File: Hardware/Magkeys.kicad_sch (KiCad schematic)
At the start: 169 parts, among them SW1 SW_Push, SW10 SW_Push, SW11 SW_Push, SW12 SW_Push, SW13 SW_Push, SW14 SW_Push, SW15 SW_Push, SW16 SW_Push, SW17 SW_Push, SW18 SW_Push, SW19 SW_Push, SW2 SW_Push, SW20 SW_Push, SW21 SW_Push, SW22 SW_Push, SW23 SW_Push, SW24 SW_Push, SW25 SW_Push, SW26 SW_Push, SW27 SW_Push, SW28 SW_Push, SW29 SW_Push, SW3 SW_Push, SW30 SW_Push, SW31 SW_Push, SW32 SW_Push, SW33 SW_Push, SW34 SW_Push, SW35 SW_Push, SW36 SW_Push, SW37 SW_Push, SW38 SW_Push, SW39 SW_Push, SW4 SW_Push, SW40 SW_Push, SW41 SW_Push, SW42 SW_Push, SW43 SW_Push, SW44 SW_Push, SW45 SW_Push, SW46 SW_Push, SW47 SW_Push, SW48 SW_Push, SW49 SW_Push, SW5 SW_Push, SW50 SW_Push, SW51 SW_Push, SW52 SW_Push, SW53 SW_Push, SW54 SW_Push, SW55 SW_Push, SW56 SW_Push, SW57 SW_Push, SW58 SW_Push, SW59 SW_Push, SW6 SW_Push, SW60 SW_Push, SW61 SW_Push, SW62 SW_Push, SW63 SW_Push, SW64 SW_Push, SW65 SW_Push, SW66 SW_Push, SW67 SW_Push, SW68 SW_Push, SW69 SW_Push, SW7 SW_Push, SW70 SW_Push, SW71 SW_Push, SW72 SW_Push, SW73 SW_Push, SW74 SW_Push, SW75 SW_Push, SW76 SW_Push, SW77 SW_Push, SW78 SW_Push, SW79 SW_Push, SW8 SW_Push, SW80 SW_Push, SW81 SW_Push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

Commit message: did layout
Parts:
- A1: footprint Module:RaspberryPi_Pico_W_SMD_HandSolder -> Module:RaspberryPi_Pico_W_SMD
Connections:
- net at D22.2 (A): now also SW22.1
- net at D6.2 (A): now also SW6.1
- net at D83.2 (A): now also SW83.1
- net at D51.2 (A): now also SW51.1
- net at D40.2 (A): now also SW40.1
- net at SW37.1: now also D37.2 (A)
- net at SW66.1: now also D66.2 (A)
- net at D36.2 (A): now also SW36.1
- net at SW55.1: now also D55.2 (A)
- net at D80.2 (A): now also SW80.1
- net at SW69.1: now also D69.2 (A)
- net at D52.2 (A): now also SW52.1
- net at SW21.1: now also D21.2 (A)
- net at SW25.1: now also D25.2 (A)
- net at SW79.1: now also D79.2 (A)
- net at SW65.1: now also D65.2 (A)
- net at SW9.1: now also D9.2 (A)
- net +3V3: now reaches A1.36 (3V3)
- net at D5.2 (A): now also SW5.1
- no-connect marks 2 -> 5
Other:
- moved on the sheet: D21, D22, D25, D36, D37, D40, D5, D51, D52, D55, D6, D65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

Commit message: idk
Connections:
- net COL1: now also A1.27 (GPIO21); no longer A1.21 (GPIO16)
- net COL2: now also A1.26 (GPIO20); no longer A1.22 (GPIO17)
- net COL3: now also A1.25 (GPIO19); no longer A1.24 (GPIO18)
- net COL4: now also A1.24 (GPIO18); no longer A1.25 (GPIO19)
- net COL5: now also A1.22 (GPIO17); no longer A1.26 (GPIO20)
- net COL6: now also A1.21 (GPIO16); no longer A1.27 (GPIO21)
- net ROW1: now also A1.20 (GPIO15); no longer A1.1 (GPIO0)
- net ROW10: now also A1.9 (GPIO6); no longer A1.12 (GPIO9)
- net ROW11: now also A1.7 (GPIO5); no longer A1.14 (GPIO10)
- net ROW12: now also A1.6 (GPIO4); no longer A1.15 (GPIO11)
- net ROW13: now also A1.5 (GPIO3); no longer A1.16 (GPIO12)
- net ROW14: now also A1.4 (GPIO2); no longer A1.17 (GPIO13)
- net ROW15: now also A1.2 (GPIO1); no longer A1.19 (GPIO14)
- net ROW16: now also A1.1 (GPIO0); no longer A1.20 (GPIO15)
- net ROW2: now also A1.19 (GPIO14); no longer A1.2 (GPIO1)
- net ROW3: now also A1.17 (GPIO13); no longer A1.4 (GPIO2)
- net ROW4: now also A1.16 (GPIO12); no longer A1.5 (GPIO3)
- net ROW5: now also A1.15 (GPIO11); no longer A1.6 (GPIO4)
- net ROW6: now also A1.14 (GPIO10); no longer A1.7 (GPIO5)
- net ROW7: now also A1.12 (GPIO9); no longer A1.9 (GPIO6)
- net ROW8: now also A1.11 (GPIO8); no longer A1.10 (GPIO7)
- net ROW9: now also A1.10 (GPIO7); no longer A1.11 (GPIO8)
- no-connect marks 5 -> 4
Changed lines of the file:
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@@
-	)
-	(no_connect
-		(at 487.68 91.44)
 	)
 	(no_connect
@@
 	)
 	(label "COL6"
-		(at 533.4 111.76 0)
+		(at 533.4 99.06 0)
 		(effects
 			(font
@@
 	)
 	(label "COL1"
-		(at 533.4 99.06 0)
+		(at 533.4 111.76 0)
 		(effects
 			(font
@@
 	)
 	(label "ROW16"
-		(at 487.68 134.62 180)
+		(at 487.68 96.52 180)
 		(effects
 			(font
@@
 	)
 	(label "ROW8"
-		(at 487.68 114.3 180)
+		(at 487.68 116.84 180)
 		(effects
 			(font
@@
 	)
 	(label "ROW14"
-		(at 487.68 129.54 180)
+		(at 487.68 101.6 180)
 		(effects
 			(font
@@
 	)
 	(label "ROW13"
-		(at 487.68 127 180)
+		(at 487.68 104.14 180)
 		(effects
 			(font
@@
 	)
 	(label "ROW6"
-		(at 487.68 109.22 180)
+		(at 487.68 121.92 180)
 		(effects
 			(font
@@
 	)
 	(label "COL2"
-		(at 533.4 101.6 0)
+		(at 533.4 109.22 0)
 		(effects
 			(font
@@
 	)
 	(label "ROW11"
-		(at 487.68 121.92 180)
+		(at 487.68 109.22 180)
 		(effects
 			(font
@@
 	)
 	(label "COL5"
-		(at 533.4 109.22 0)
+		(at 533.4 101.6 0)
 		(effects
 			(font
@@
 	)
 	(label "COL3"
-		(at 533.4 104.14 0)
+		(at 533.4 106.68 0)
 		(effects
 			(font
@@
 	)
 	(label "ROW10"
-		(at 487.68 119.38 180)
+		(at 487.68 111.76 180)
 		(effects
 			(font
@@
 	)
 	(label "ROW4"
-		(at 487.68 104.14 180)
+		(at 487.68 127 180)
 		(effects
 			(font
@@
 	)
 	(label "ROW12"
-		(at 487.68 124.46 180)
+		(at 487.68 106.68 180)
 		(effects
 			(font
@@
 	)
 	(label "ROW15"
-		(at 487.68 132.08 180)
+		(at 487.68 99.06 180)
 		(effects
 			(font
@@
 	)
 	(label "ROW9"
-		(at 487.68 116.84 180)
+		(at 487.68 114.3 180)
 		(effects
 			(font
@@
 	)
 	(label "ROW7"
-		(at 487.68 111.76 180)
+		(at 487.68 119.38 180)
 		(effects
 			(font
@@
 	)
 	(label "ROW3"
-		(at 487.68 101.6 180)
+		(at 487.68 129.54 180)
 		(effects
 			(font
@@
 	)
 	(label "ROW1"
-		(at 487.68 96.52 180)
+		(at 487.68 134.62 180)
 		(effects
 			(font
@@
 	)
 	(label "COL4"
-		(at 533.4 106.68 0)
+		(at 533.4 104.14 0)
 		(effects
 			(font
@@
 	)
 	(label "ROW2"
-		(at 487.68 99.06 180)
+		(at 487.68 132.08 180)
 		(effects
 			(font
@@
 	)
 	(label "ROW5"
-		(at 487.68 106.68 180)
-		(effects
-			(font
+		(at 487.68 124.46 180)
+		(effects
+			(font

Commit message: Added numpad
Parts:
- added D100, D101, D85, D86, D87, D88, D89, D90, D91, D92, D93, D94, D95, D96, D97, D98, D99: 1N4148W, Diode_SMD:D_SOD-123, symbol Diode:1N4148W
- added SW100: SW_Push, Button_Switch_Keyboard:SW_Cherry_MX_2.00u_Plate, symbol Switch:SW_Push
- added SW101, SW85, SW86, SW87, SW88, SW89, SW90, SW91, SW93, SW94, SW95, SW96, SW97, SW98: SW_Push, Button_Switch_Keyboard:SW_Cherry_MX_1.00u_Plate, symbol Switch:SW_Push
- added SW92, SW99: SW_Push, Button_Switch_Keyboard:SW_Cherry_MX_2.00u_Vertical_Plate, symbol Switch:SW_Push
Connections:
- new net: D89.2 (A), SW89.1
- new net: D100.2 (A), SW100.1
- new net: D97.2 (A), SW97.1
- new net: D85.2 (A), SW85.1
- new net: D101.2 (A), SW101.1
- new net: D94.2 (A), SW94.1
- new net: D93.2 (A), SW93.1
- new net: D96.2 (A), SW96.1
- new net: D91.2 (A), SW91.1
- new net: D90.2 (A), SW90.1
- new net: D87.2 (A), SW87.1
- new net: D95.2 (A), SW95.1
- new net: D88.2 (A), SW88.1
- new net: D99.2 (A), SW99.1
- new net: D86.2 (A), SW86.1
- new net: D92.2 (A), SW92.1
- new net: D98.2 (A), SW98.1
- new net NUM_COL1: SW100.2, SW85.2, SW89.2, SW93.2, SW96.2
- new net NUM_COL2: SW101.2, SW86.2, SW90.2, SW94.2, SW97.2
- new net NUM_COL3: SW87.2, SW91.2, SW95.2, SW98.2
- new net NUM_COL4: SW88.2, SW92.2, SW99.2
- new net NUM_ROW1: D85.1 (K), D86.1 (K), D87.1 (K), D88.1 (K)
- new net NUM_ROW2: D89.1 (K), D90.1 (K), D91.1 (K), D92.1 (K)
- new net NUM_ROW3: D93.1 (K), D94.1 (K), D95.1 (K)
- new net NUM_ROW4: D96.1 (K), D97.1 (K), D98.1 (K), D99.1 (K)
- new net NUM_ROW5: D100.1 (K), D101.1 (K)
- no-connect marks 4 -> 5
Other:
- moved on the sheet: A1

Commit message: Completed PCB
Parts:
- added U1: Seeeduino Xiao rp2040, PCM_marbastlib-xp-promicroish:Xiao_rp2040_AC_Reflow, symbol PCM_marbastlib-promicroish:Seeeduino_Xiao_rp2040
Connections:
- net +3V3: now also U1.10 (3V3)
- net GND: now also U1.18 (GND), U1.22 (GND), U1.9 (GND)
- net NUM_COL1: now also U1.11 (P3)
- net NUM_COL2: now also U1.12 (P4)
- net NUM_COL3: now also U1.13 (P2)
- net NUM_COL4: now also U1.14 (P1)
- net NUM_ROW1: now also U1.3 (P28)
- net NUM_ROW2: now also U1.4 (P29)
- net NUM_ROW3: now also U1.5 (P6)
- net NUM_ROW4: now also U1.6 (P7)
- net NUM_ROW5: now also U1.7 (P0)
- net VBUS: now also U1.17 (VIN)
- new net +5V: U1.8 (5V)
- no-connect marks 5 -> 8

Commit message: changes in the PCB
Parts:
- removed U1: Seeeduino Xiao rp2040, PCM_marbastlib-xp-promicroish:Xiao_rp2040_AC_Reflow, symbol PCM_marbastlib-promicroish:Seeeduino_Xiao_rp2040
- added J1: Conn_01x04_Pin, Connector_PinHeader_2.54mm:PinHeader_1x04_P2.54mm_Vertical, symbol Connector:Conn_01x04_Pin
- added SW102: RotaryEncoder, Rotary_Encoder:RotaryEncoder_Alps_EC11E_Vertical_H20mm, symbol Device:RotaryEncoder
- SW1, SW10, SW101, SW11, SW12, SW13, SW14, SW15, SW16, SW17, SW18, SW19, SW2, SW20, SW21, SW22, SW23, SW24, SW25, SW26, SW27, SW28, SW29, SW3, SW31, SW33, SW34, SW35, SW36, SW37, SW38, SW39, SW4, SW40, SW41, SW42, SW43, SW44, SW46, SW48, SW49, SW5, SW50, SW51, SW52, SW53, SW54, SW55, SW56, SW57, SW58, SW6, SW60, SW62, SW63, SW64, SW65, SW66, SW67, SW68, SW69, SW7, SW70, SW71, SW73, SW74, SW79, SW8, SW80, SW81, SW82, SW83, SW84, SW85, SW86, SW87, SW88, SW89, SW9, SW90, SW91, SW93, SW94, SW95, SW96, SW97, SW98: footprint Button_Switch_Keyboard:SW_Cherry_MX_1.00u_Plate -> easyeda2kicad:SW_Cherry_MX_1.00u_Plate
- SW100, SW30: footprint Button_Switch_Keyboard:SW_Cherry_MX_2.00u_Plate -> easyeda2kicad:SW_Cherry_MX_2.00u_Plate
- SW32, SW45: footprint Button_Switch_Keyboard:SW_Cherry_MX_1.50u_Plate -> easyeda2kicad:SW_Cherry_MX_1.50u_Plate
- SW47, SW72: footprint Button_Switch_Keyboard:SW_Cherry_MX_1.75u_Plate -> easyeda2kicad:SW_Cherry_MX_1.75u_Plate
- SW59, SW61: footprint Button_Switch_Keyboard:SW_Cherry_MX_2.25u_Plate -> easyeda2kicad:SW_Cherry_MX_2.25u_Plate
- SW75, SW76, SW77: footprint Button_Switch_Keyboard:SW_Cherry_MX_1.25u_Plate -> easyeda2kicad:SW_Cherry_MX_1.25u_Plate
- SW78: footprint Button_Switch_Keyboard:SW_Cherry_MX_6.25u_Plate -> easyeda2kicad:SW_Cherry_MX_6.25u_Plate
- SW92, SW99: footprint Button_Switch_Keyboard:SW_Cherry_MX_2.00u_Vertical_Plate -> easyeda2kicad:SW_Cherry_MX_2.00u_Vertical_Plate
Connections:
- net COL1: now also A1.31 (GPIO26_ADC0); no longer A1.27 (GPIO21)
- net COL2: now also A1.29 (GPIO22); no longer A1.26 (GPIO20)
- net COL3: now also A1.27 (GPIO21); no longer A1.25 (GPIO19)
- net COL4: now also A1.26 (GPIO20); no longer A1.24 (GPIO18)
- net COL5: now also A1.25 (GPIO19); no longer A1.22 (GPIO17)
- net COL6: now also A1.24 (GPIO18); no longer A1.21 (GPIO16)
- net GND: now also J1.4 (Pin_4), SW102.C
- net VBUS: now also J1.1 (Pin_1)
- net ENC_A: now reaches A1.32 (GPIO27_ADC1)
- net ENC_A: now also SW102.A
- net ENC_B: now reaches A1.34 (GPIO28_ADC2)
- net ENC_B: now also SW102.B
- new net U0_RX: A1.22 (GPIO17), J1.3 (Pin_3)
- new net U0_TX: A1.21 (GPIO16), J1.2 (Pin_2)
- no-connect marks 8 -> 4

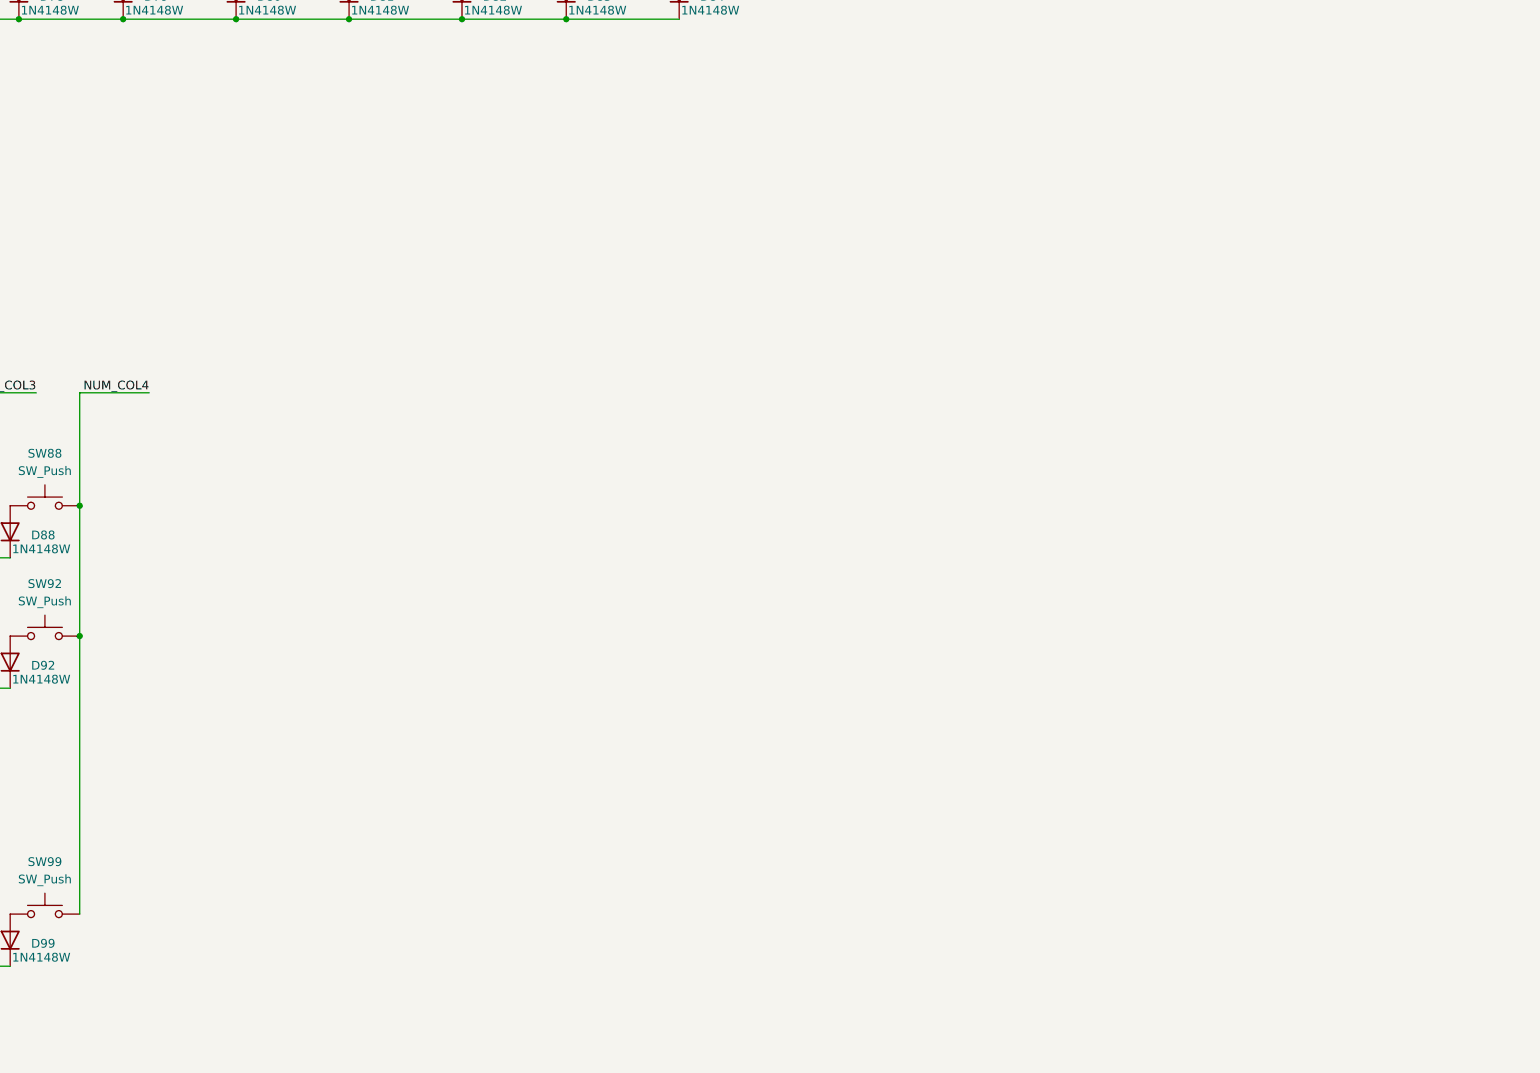
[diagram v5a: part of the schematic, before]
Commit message: new mcu
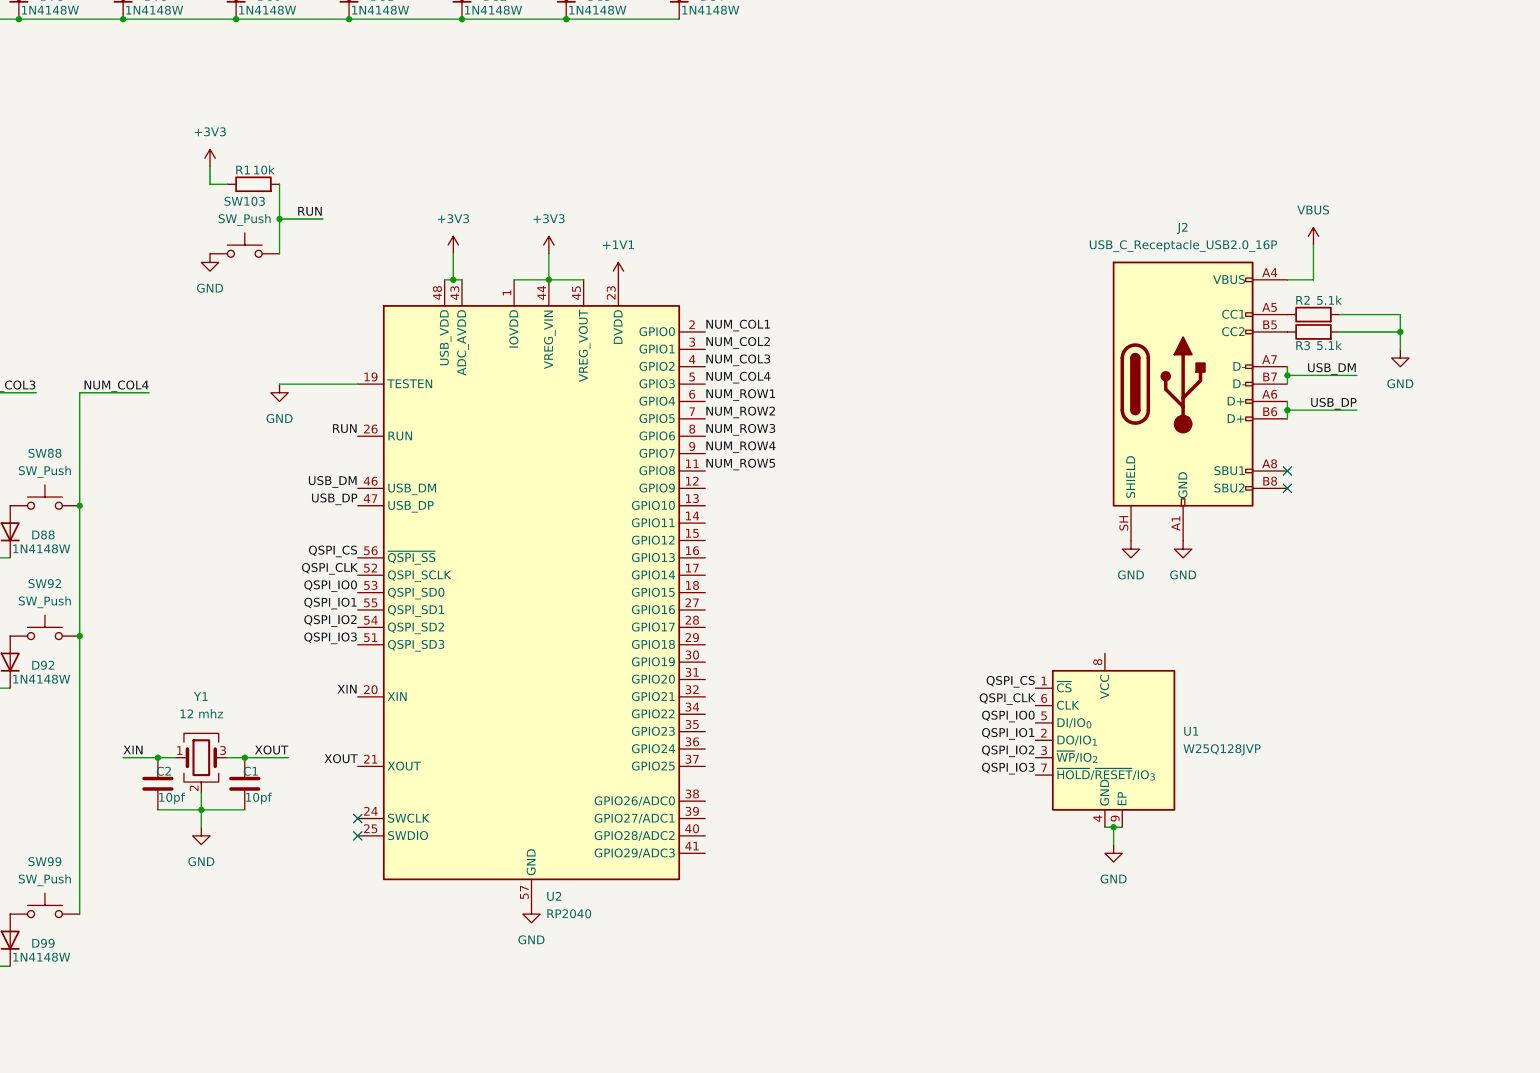
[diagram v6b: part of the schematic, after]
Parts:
- added C1, C2: 10pf, symbol Device:C
- added J2: USB_C_Receptacle_USB2.0_16P, symbol Connector:USB_C_Receptacle_USB2.0_16P
- added R1: 10k, symbol Device:R
- added R2, R3: 5.1k, symbol Device:R
- added SW103: SW_Push, symbol Switch:SW_Push
- added U1: W25Q128JVP, Package_SON:WSON-8-1EP_6x5mm_P1.27mm_EP3.4x4.3mm, symbol Memory_Flash:W25Q128JVP
- added U2: RP2040, Package_DFN_QFN:QFN-56-1EP_7x7mm_P0.4mm_EP3.2x3.2mm, symbol MCU_RaspberryPi:RP2040
- added Y1: 12 mhz, symbol Device:Crystal_GND24
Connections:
- net +3V3: now also R1.1, U2.1 (IOVDD), U2.10 (IOVDD), U2.22 (IOVDD), U2.33 (IOVDD), U2.42 (IOVDD), U2.43 (ADC_AVDD), U2.44 (VREG_VIN), U2.45 (VREG_VOUT), U2.48 (USB_VDD), U2.49 (IOVDD)
- net GND: now also C1.2, C2.2, J2.A1 (GND), J2.A12 (GND), J2.B1 (GND), J2.B12 (GND), J2.SH (SHIELD), R2.2, R3.2, SW103.1, U1.4 (GND), U1.9 (EP), U2.19 (TESTEN), U2.57 (GND), Y1.2 (G), Y1.4 (G)
- net NUM_COL1: now also U2.2 (GPIO0)
- net NUM_COL2: now also U2.3 (GPIO1)
- net NUM_COL3: now also U2.4 (GPIO2)
- net NUM_COL4: now also U2.5 (GPIO3)
- net NUM_ROW1: now also U2.6 (GPIO4)
- net NUM_ROW2: now also U2.7 (GPIO5)
- net NUM_ROW3: now also U2.8 (GPIO6)
- net NUM_ROW4: now also U2.9 (GPIO7)
- net NUM_ROW5: now also U2.11 (GPIO8)
- net VBUS: now also J2.A4 (VBUS), J2.A9 (VBUS), J2.B4 (VBUS), J2.B9 (VBUS)
- new net: J2.A5 (CC1), R2.1
- new net: J2.B5 (CC2), R3.1
- new net +1V1: U2.23 (DVDD), U2.50 (DVDD)
- new net QSPI_CLK: U1.6 (CLK), U2.52 (QSPI_SCLK)
- new net QSPI_CS: U1.1 (~{CS}), U2.56 (~{QSPI_SS})
- new net QSPI_IO0: U1.5 (DI/IO_{0}), U2.53 (QSPI_SD0)
- new net QSPI_IO1: U1.2 (DO/IO_{1}), U2.55 (QSPI_SD1)
- new net QSPI_IO2: U1.3 (~{WP}/IO_{2}), U2.54 (QSPI_SD2)
- new net QSPI_IO3: U1.7 (~{HOLD}/~{RESET}/IO_{3}), U2.51 (QSPI_SD3)
- new net RUN: R1.2, SW103.2, U2.26 (RUN)
- new net USB_DM: J2.A7 (D-), J2.B7 (D-), U2.46 (USB_DM)
- new net USB_DP: J2.A6 (D+), J2.B6 (D+), U2.47 (USB_DP)
- new net XIN: C2.1, U2.20 (XIN), Y1.1
- new net XOUT: C1.1, U2.21 (XOUT), Y1.3
- no-connect marks 4 -> 8

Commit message: 3d files generated, PCB updated and production files generated too
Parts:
- removed SW102: RotaryEncoder, Rotary_Encoder:RotaryEncoder_Alps_EC11E_Vertical_H20mm, symbol Device:RotaryEncoder
- removed SW103: SW_Push, symbol Switch:SW_Push
- added C10: 1u, Capacitor_SMD:C_0402_1005Metric, symbol Device:C_Small
- added C11, C12, C13, C3, C4, C5, C6, C7, C8, C9: 100n, Capacitor_SMD:C_0402_1005Metric, symbol Device:C_Small
- added C14, C15: 10u, Capacitor_SMD:C_0402_1005Metric, symbol Device:C_Small
- added H1, H2, H3, H4, H5, H6, H7, H8: MountingHole, MountingHole:MountingHole_3.2mm_M3, symbol Mechanical:MountingHole
- added J3: Conn_01x04_Pin, Connector_PinHeader_2.54mm:PinHeader_1x04_P2.54mm_Vertical, symbol Connector:Conn_01x04_Pin
- added JP1: Jumper_2_Open, Jumper:SolderJumper-2_P1.3mm_Open_TrianglePad1.0x1.5mm, symbol Jumper:Jumper_2_Open
- added L1: 1u, Inductor_SMD:L_0402_1005Metric, symbol Device:L
- added R4, R5: 27, Resistor_SMD:R_0402_1005Metric, symbol Device:R_Small
- added R6: 1k, Resistor_SMD:R_0402_1005Metric, symbol Device:R_Small
- added R7: 10k, Resistor_SMD:R_0402_1005Metric, symbol Device:R
- added SW103: RotaryEncoder_Switch_MP, Rotary_Encoder:RotaryEncoder_Alps_EC11E-Switch_Vertical_H20mm_MountingHoles, symbol Device:RotaryEncoder_Switch_MP
- added SW104: SW_Push, Button_Switch_SMD:SW_SPST_PTS810, symbol Switch:SW_Push
- added U3: ADP2108AUJ-3.3, Package_TO_SOT_SMD:TSOT-23-5, symbol Regulator_Switching:ADP2108AUJ-3.3
- C1, C2: value 10pf -> 15p; footprint (none) -> Capacitor_SMD:C_0402_1005Metric
- J2: footprint (none) -> Connector_USB:USB_C_Receptacle_XKB_U262-16XN-4BVC11
- R1, R2, R3: footprint (none) -> Resistor_SMD:R_0402_1005Metric
- Y1: value 12 mhz -> 12 MHz; footprint (none) -> Crystal:Crystal_SMD_3225-4Pin_3.2x2.5mm
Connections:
- net +1V1: now also U2.45 (VREG_VOUT), C11.1, C12.1, C13.1
- net +3V3: now also U1.8 (VCC), C10.1, C15.1, C3.1, C4.1, C5.1, C6.1, C7.1, C8.1, C9.1, L1.2, R7.1, U3.4 (FB); no longer U2.45 (VREG_VOUT)
- net ENC_A: now also U2.30 (GPIO19), SW103.A; no longer A1.32 (GPIO27_ADC1)
- net ENC_B: now also U2.29 (GPIO18), SW103.B; no longer A1.34 (GPIO28_ADC2)
- net GND: now also C10.2, C11.2, C12.2, C13.2, C14.2, C15.2, C3.2, C4.2, C5.2, C6.2, C7.2, C8.2, C9.2, J3.4 (Pin_4), JP1.1 (A), SW103.C, SW103.MP, SW104.1, U3.2 (GND)
- net NUM_COL3: now also U2.5 (GPIO3); no longer U2.4 (GPIO2)
- net NUM_COL4: now also U2.4 (GPIO2); no longer U2.5 (GPIO3)
- net NUM_ROW1: now also U2.11 (GPIO8); no longer U2.6 (GPIO4)
- net NUM_ROW2: now also U2.9 (GPIO7); no longer U2.7 (GPIO5)
- net NUM_ROW4: now also U2.7 (GPIO5); no longer U2.9 (GPIO7)
- net NUM_ROW5: now also U2.6 (GPIO4); no longer U2.11 (GPIO8)
- net QSPI_CS: now also R7.2, SW104.2
- net RUN: now also JP1.2 (B)
- net USB_DP: now also R4.2; no longer U2.47 (USB_DP)
- net VBUS: now also C14.1, J3.1 (Pin_1), U3.1 (Vin), U3.3 (EN)
- net XOUT: now also R6.2; no longer U2.21 (XOUT)
- net U00_TX: now reaches U2.15 (GPIO12)
- net U00_TX: now also J3.3 (Pin_3)
- net U00_RX: now reaches U2.16 (GPIO13)
- net U00_RX: now also J3.2 (Pin_2)
- net ENC_S1: now reaches U2.36 (GPIO24)
- net ENC_S1: now also SW103.S1
- net ENC_S2: now reaches U2.37 (GPIO25)
- net ENC_S2: now also SW103.S2
- net USB_DM renamed USB_DN
- net USB_DN: now also R5.2; no longer U2.46 (USB_DM)
- new net: L1.1, U3.5 (SW)
- new net: R6.1, U2.21 (XOUT)
- new net USB_F_DN: R5.1, U2.46 (USB_DM)
- new net USB_F_DP: R4.1, U2.47 (USB_DP)
- no-connect marks 8 -> 12
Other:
- moved on the sheet: C1, C2, Y1
